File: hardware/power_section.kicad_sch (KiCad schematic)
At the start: 33 parts, among them J3 Conn_01x02, J3 USB_C_Receptacle_USB2.0, SW7 SW_SPDT, U3 AMS1117-3.3, U3 DW01A, U4 FS8502A, U5 TP4056, U6 SDB628

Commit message: Finished power section
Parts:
- removed J3: USB_C_Receptacle_USB2.0, Connector_USB:USB_C_Receptacle_XKB_U262-16XN-4BVC11, symbol Connector:USB_C_Receptacle_USB2.0
- removed U3: DW01A, Package_TO_SOT_SMD:SOT-23-6, symbol newsymbols:DW01A
- removed U4: FS8502A, Package_SO:TSSOP-8_4.4x3mm_P0.65mm, symbol newsymbols:FS8502A
- removed U5: TP4056, Package_SO:SOIC-8-1EP_3.9x4.9mm_P1.27mm_EP2.29x3mm_ThermalVias, symbol newsymbols:TP4056
- removed U6: SDB628, Package_TO_SOT_SMD:SOT-23-6, symbol newsymbols:SDB628
- added C12, C18: 15p, Capacitor_SMD:C_0603_1608Metric, symbol Device:C
- added J6: USB_C_Receptacle_USB2.0_16P, Connector_USB:USB_C_Receptacle_XKB_U262-16XN-4BVC11, symbol Connector:USB_C_Receptacle_USB2.0_16P
- added R8, R9: 5.1k, Resistor_SMD:R_0603_1608Metric, symbol Device:R
- added U4: FS8502A, Package_SO:TSSOP-8_4.4x3mm_P0.65mm, symbol additional_symbols:FS8502A
- added U5: TP4056, Package_SO:SOIC-8-1EP_3.9x4.9mm_P1.27mm_EP2.29x3mm_ThermalVias, symbol additional_symbols:TP4056
- added U6: HX3242, Package_SO:SOP-8-1EP_4.57x4.57mm_P1.27mm_EP4.57x4.45mm, symbol additional_symbols:HX3242
- added U9: DW01A, Package_TO_SOT_SMD:SOT-23-6, symbol additional_symbols:DW01A
- L1: value 22u -> 4.7u; footprint Inductor_SMD:L_0805_2012Metric -> Inductor_SMD:L_7.3x7.3_H3.5
- R2: value 390k -> 33k; footprint Resistor_SMD:R_0603_1608Metric -> Resistor_SMD:R_0805_2012Metric
- R2: value 51k -> 10k; footprint Resistor_SMD:R_0603_1608Metric -> Resistor_SMD:R_0805_2012Metric
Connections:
- net +5V: now also D1.1 (K), U6.6 (VDD); no longer D1.2 (A)
- net +BATT: now also U5.5 (BAT)
- net -BATT: now also U4.2 (S1), U4.3 (S1), U9.6 (GND)
- net 5V enable: now also C18.2, U6.7 (EN)
- net GND: now also C12.1, C18.1, J6.A1 (GND), J6.A12 (GND), J6.B1 (GND), J6.B12 (GND), J6.S1 (SHIELD), R8.2, R9.2, U4.6 (S2), U4.7 (S2), U5.1 (TEMP), U5.3 (GND), U5.9 (GND), U6.3 (SOE), U6.4 (SOE), U6.5 (GND)
- net VBUS: now also J6.A4 (VBUS), J6.A9 (VBUS), J6.B4 (VBUS), J6.B9 (VBUS), U5.4 (Vcc), U5.8 (CE)
- net at R7.1: now also U5.2 (PROG)
- net at R6.2: now also U5.6 (~{STDBY})
- net at R5.2: now also U5.7 (~{CHRG})
- net at C1.2, R3.2: now also U9.5 (VCC)
- net at R2.1, R2.2: now also C12.2, U6.8 (FB)
- net at L1.2: now also D1.2 (A), U6.1 (SW), U6.2 (SW); no longer D1.1 (K)
- net at R4.1: now also U9.2 (CS)
- new net: J6.A5 (CC1), R9.1
- new net: J6.A6 (D+), J6.B6 (D+)
- new net: J6.A7 (D-), J6.B7 (D-)
- new net: J6.B5 (CC2), R8.1
- new net: U4.4 (G1), U9.1 (OD)
- new net: U4.5 (G2), U9.3 (OC)
- no-connect marks 12 -> 6
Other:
- note removed: "TODO USB C 5V mode"
- moved on the sheet: BT1, C1, C10, C11, C2, C3, C4, C5, C6, C7, C8, C9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

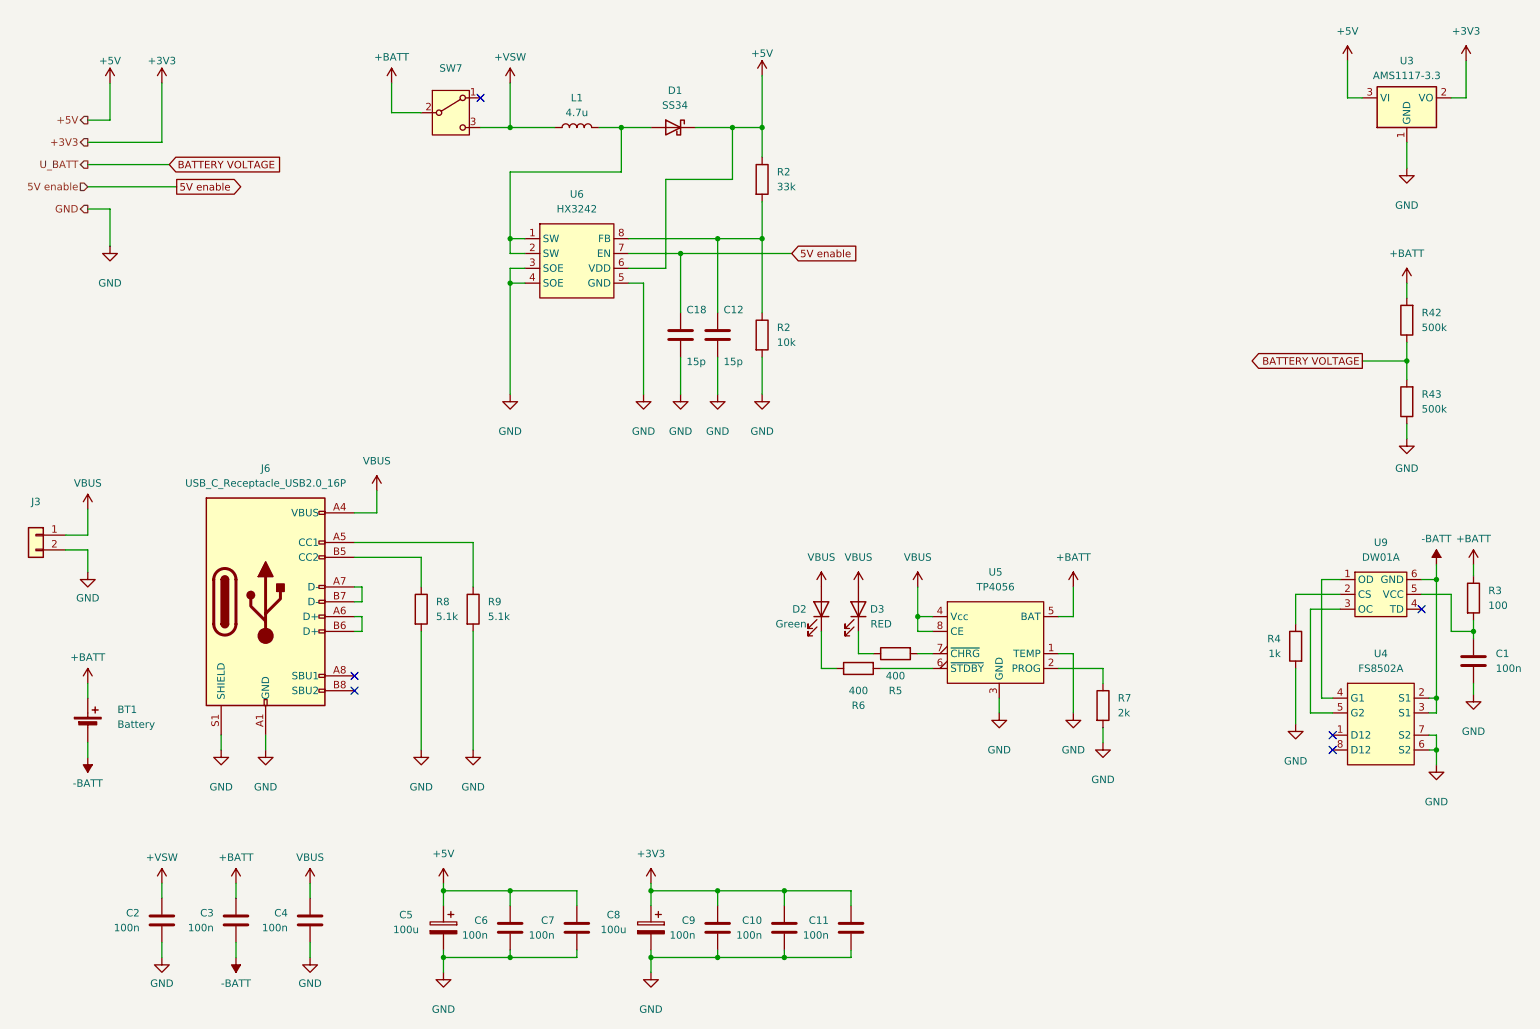
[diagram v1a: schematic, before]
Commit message: Human Interface section finished
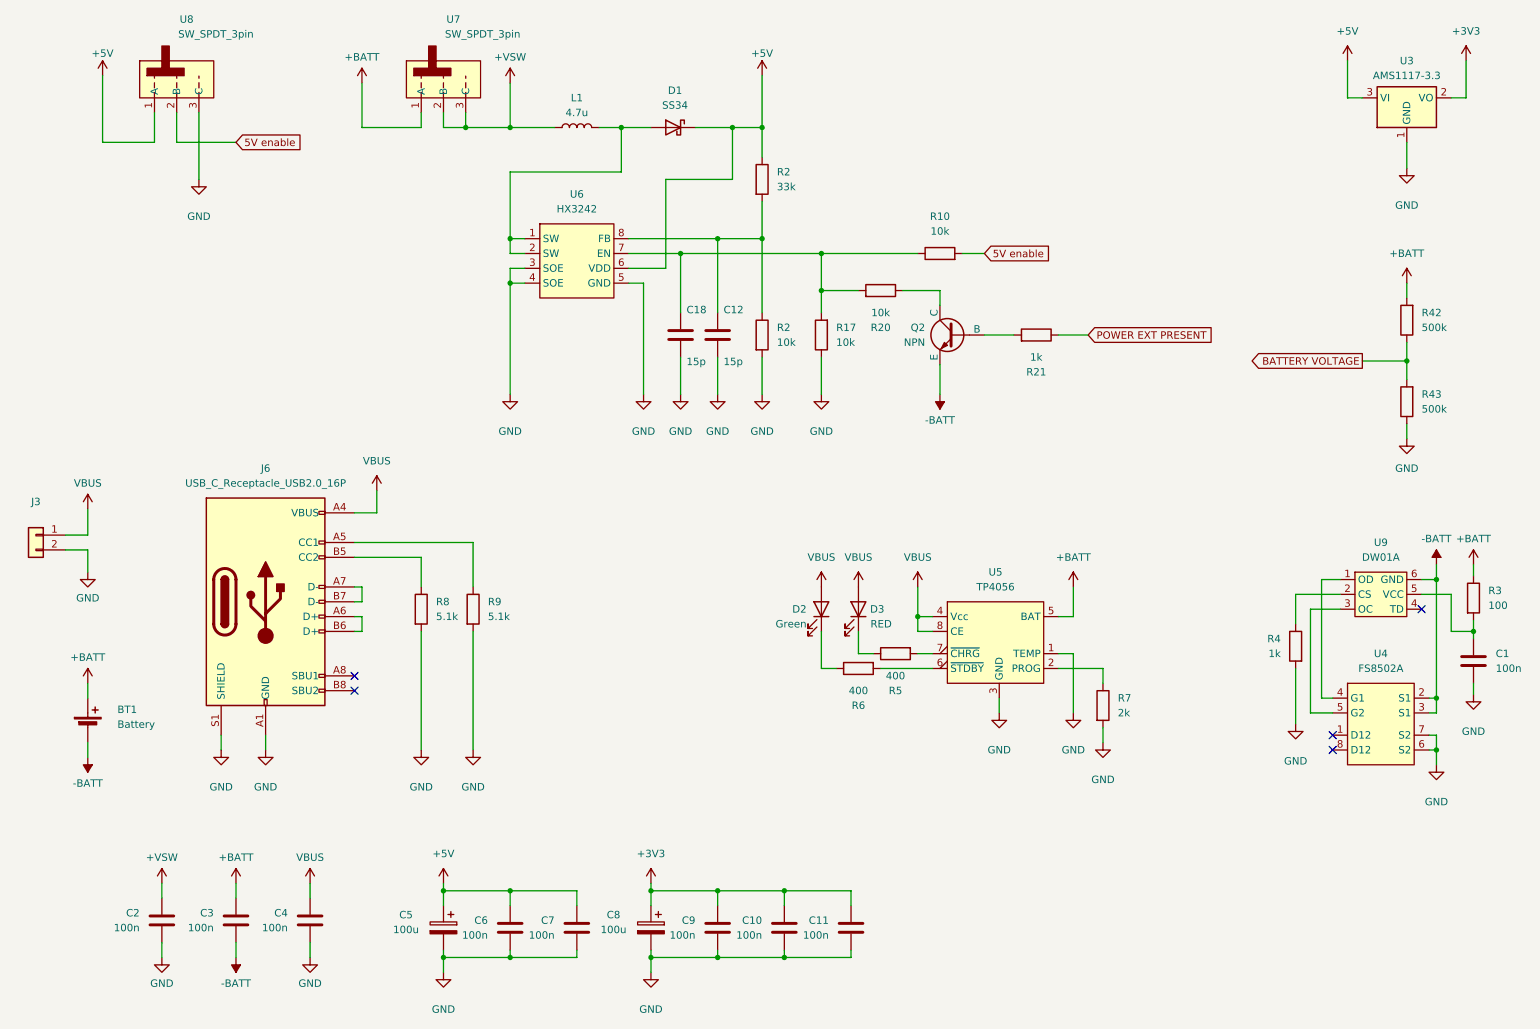
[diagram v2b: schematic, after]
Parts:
- removed SW7: SW_SPDT, work:SW_Slide_SPDT_wo_mount, symbol Switch:SW_SPDT
- added Q2: NPN, symbol Simulation_SPICE:NPN
- added R10, R17, R20: 10k, Resistor_SMD:R_0603_1608Metric, symbol Device:R
- added R21: 1k, Resistor_SMD:R_0603_1608Metric, symbol Device:R
- added U7, U8: SW_SPDT_3pin, additional_footprints:my_switch, symbol additional_symbols:SW_SPDT_3pin
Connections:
- net +5V: now also U8.1 (A)
- net +BATT: now also U7.1 (A)
- net +VSW: now also U7.2 (B), U7.3 (C)
- net -BATT: now also Q2.3 (E)
- net 5V enable: now also R10.2, U8.2 (B); no longer C18.2, U6.7 (EN)
- net GND: now also R17.1, U8.3 (C)
- new net: C18.2, R10.1, R17.2, R20.2, U6.7 (EN)
- new net: Q2.2 (B), R21.2
- new net: Q2.1 (C), R20.1
- new net POWER EXT PRESENT: R21.1
- no-connect marks 6 -> 5

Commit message: Moved MCU to general section
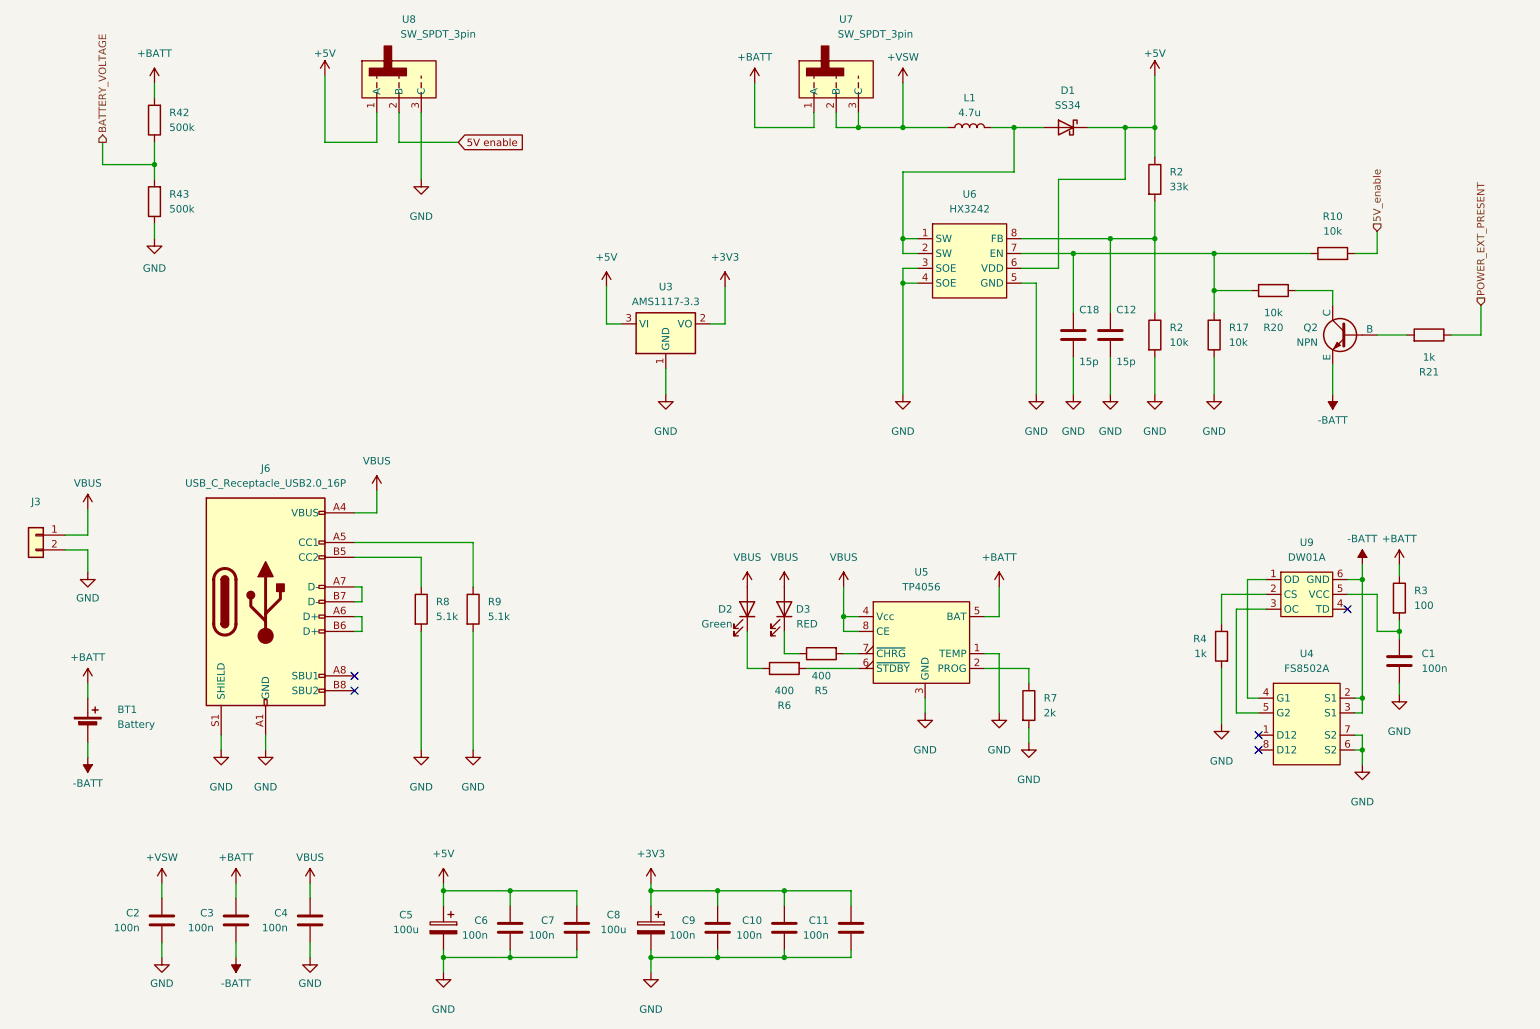
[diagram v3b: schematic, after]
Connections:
- net 5V enable: no longer R10.2
- net BATTERY VOLTAGE renamed BATTERY_VOLTAGE
- net POWER EXT PRESENT renamed POWER_EXT_PRESENT
- new net 5V_enable: R10.2
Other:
- moved on the sheet: C1, C12, C18, D1, D2, D3, L1, Q2, R10, R17, R2, R20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
